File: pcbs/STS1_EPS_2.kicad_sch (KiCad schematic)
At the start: 8 parts, among them J1 Inter-EPS, J2 DS1, J3 DS2, J4 DS3, J5 DS4, J6 RBF, J7 Antenna Deployment, J8 UCI

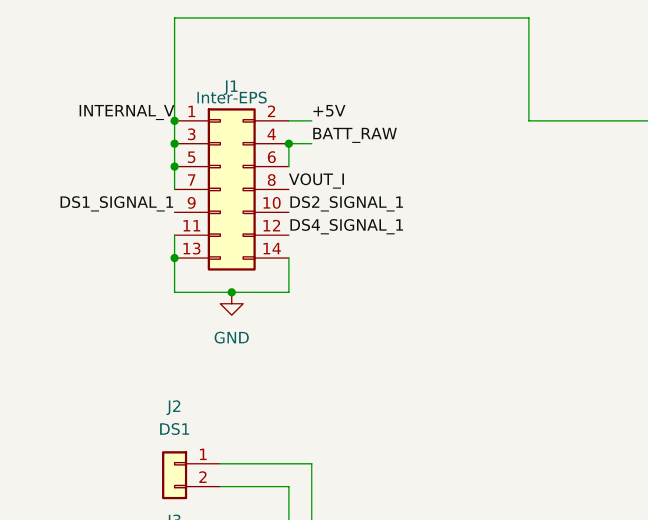
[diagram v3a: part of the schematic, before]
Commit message: Made STS1_EPS_2 inter EPS connector consistent to STS1_EPS_1.
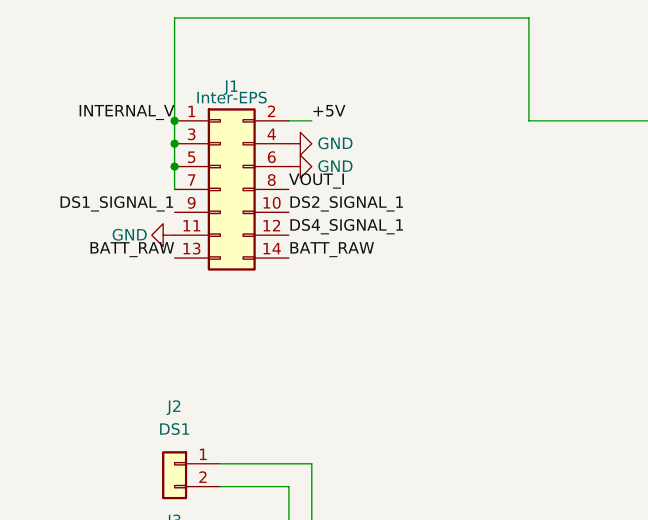
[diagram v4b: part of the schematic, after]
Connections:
- net BATT_RAW: now also J1.13 (Pin_13), J1.14 (Pin_14); no longer J1.4 (Pin_4), J1.6 (Pin_6)
- net GND: now also J1.4 (Pin_4), J1.6 (Pin_6); no longer J1.13 (Pin_13), J1.14 (Pin_14)
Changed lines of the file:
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@@
 (kicad_sch (version 20211123) (generator eeschema)
   (paper "A4")
-  (junction (at 40.64 45.72) (diameter 0) (color 0 0 0 0)
-  )
-  (junction (at 27.94 58.42) (diameter 0) (color 0 0 0 0)
-  )
   (junction (at 27.94 48.26) (diameter 0) (color 0 0 0 0)
   )
@@
   )
   (junction (at 27.94 43.18) (diameter 0) (color 0 0 0 0)
-  )
-  (junction (at 34.29 62.23) (diameter 0) (color 0 0 0 0)
   )
   (no_connect (at 43.18 185.42))
@@
     (stroke (width 0) (type default) (color 0 0 0 0))
   )
-  (wire (pts (xy 27.94 62.23) (xy 34.29 62.23))
-    (stroke (width 0) (type default) (color 0 0 0 0))
-  )
   (wire (pts (xy 40.64 43.18) (xy 43.18 43.18))
     (stroke (width 0) (type default) (color 0 0 0 0))
   )
-  (wire (pts (xy 27.94 58.42) (xy 27.94 62.23))
-    (stroke (width 0) (type default) (color 0 0 0 0))
-  )
   (wire (pts (xy 33.02 109.22) (xy 49.53 109.22))
     (stroke (width 0) (type default) (color 0 0 0 0))
@@
     (stroke (width 0) (type default) (color 0 0 0 0))
   )
-  (wire (pts (xy 43.18 45.72) (xy 40.64 45.72))
-    (stroke (width 0) (type default) (color 0 0 0 0))
-  )
   (wire (pts (xy 27.94 43.18) (xy 27.94 31.75))
     (stroke (width 0) (type default) (color 0 0 0 0))
@@
     (stroke (width 0) (type default) (color 0 0 0 0))
   )
-  (wire (pts (xy 27.94 55.88) (xy 27.94 58.42))
-    (stroke (width 0) (type default) (color 0 0 0 0))
-  )
-  (wire (pts (xy 40.64 58.42) (xy 40.64 62.23))
-    (stroke (width 0) (type default) (color 0 0 0 0))
-  )
   (wire (pts (xy 33.02 121.92) (xy 38.1 121.92))
     (stroke (width 0) (type default) (color 0 0 0 0))
@@
     (stroke (width 0) (type default) (color 0 0 0 0))
   )
-  (wire (pts (xy 40.64 62.23) (xy 34.29 62.23))
-    (stroke (width 0) (type default) (color 0 0 0 0))
-  )
   (wire (pts (xy 33.02 96.52) (xy 35.56 96.52))
     (stroke (width 0) (type default) (color 0 0 0 0))
   )
-  (wire (pts (xy 40.64 45.72) (xy 40.64 48.26))
-    (stroke (width 0) (type default) (color 0 0 0 0))
-  )
   (wire (pts (xy 40.64 120.65) (xy 49.53 120.65))
     (stroke (width 0) (type default) (color 0 0 0 0))
@@
     (effects (font (size 1.27 1.27)) (justify left bottom))
   )
+  (label "BATT_RAW" (at 40.64 58.42 0)
+    (effects (font (size 1.27 1.27)) (justify left bottom))
+  )
   (label "DS3_SIGNAL_2" (at 78.74 111.76 0)
     (effects (font (size 1.27 1.27)) (justify left bottom))
   )
-  (label "BATT_RAW" (at 43.18 45.72 0)
-    (effects (font (size 1.27 1.27)) (justify left bottom))
-  )
   (label "UCI_COBC_UART_[1..2]" (at 240.03 53.34 180)
     (effects (font (size 1.27 1.27)) (justify right bottom))
@@
   )
   (label "DS3_SIGNAL_1" (at 168.91 49.53 180)
+    (effects (font (size 1.27 1.27)) (justify right bottom))
+  )
+  (label "BATT_RAW" (at 27.94 58.42 180)
     (effects (font (size 1.27 1.27)) (justify right bottom))
   )
@@
     (pin "4")
   )
-  (symbol (lib_id "power:GND") (at 34.29 62.23 0) (unit 1)
+  (symbol (lib_id "power:GND") (at 40.64 48.26 90) (unit 1)
     (in_bom yes) (on_board yes) (fields_autoplaced)
-    (property "Reference" "#PWR0101" (id 0) (at 34.29 68.58 0)
-      (effects (font (size 1.27 1.27)) hide)
-    )
-    (property "Value" "GND" (id 1) (at 34.29 67.31 0))
-    (property "Footprint" "" (id 2) (at 34.29 62.23 0)
-      (effects (font (size 1.27 1.27)) hide)
-    )
-    (property "Datasheet" "" (id 3) (at 34.29 62.23 0)
+    (property "Reference" "#PWR?" (id 0) (at 46.99 48.26 0)
+      (effects (font (size 1.27 1.27)) hide)
+    )
+    (property "Value" "GND" (id 1) (at 43.815 48.2599 90)
+      (effects (font (size 1.27 1.27)) (justify right))
+    )
+    (property "Footprint" "" (id 2) (at 40.64 48.26 0)
+      (effects (font (size 1.27 1.27)) hide)
+    )
+    (property "Datasheet" "" (id 3) (at 40.64 48.26 0)
+      (effects (font (size 1.27 1.27)) hide)
+    )
+    (pin "1")
+  )
+  (symbol (lib_id "power:GND") (at 40.64 45.72 90) (unit 1)
+    (in_bom yes) (on_board yes) (fields_autoplaced)
+    (property "Reference" "#PWR?" (id 0) (at 46.99 45.72 0)
+      (effects (font (size 1.27 1.27)) hide)
+    )
+    (property "Value" "GND" (id 1) (at 43.815 45.7199 90)
+      (effects (font (size 1.27 1.27)) (justify right))
+    )
+    (property "Footprint" "" (id 2) (at 40.64 45.72 0)
+      (effects (font (size 1.27 1.27)) hide)
+    )
+    (property "Datasheet" "" (id 3) (at 40.64 45.72 0)
       (effects (font (size 1.27 1.27)) hide)
     )
@@
     (pin "2")
   )
+  (symbol (lib_id "power:GND") (at 27.94 55.88 270) (unit 1)
+    (in_bom yes) (on_board yes)
+    (property "Reference" "#PWR?" (id 0) (at 21.59 55.88 0)
+      (effects (font (size 1.27 1.27)) hide)
+    )
+    (property "Value" "GND" (id 1) (at 20.955 55.88 90)
+      (effects (font (size 1.27 1.27)) (justify left))
+    )
+    (property "Footprint" "" (id 2) (at 27.94 55.88 0)
+      (effects (font (size 1.27 1.27)) hide)
+    )
+    (property "Datasheet" "" (id 3) (at 27.94 55.88 0)
+      (effects (font (size 1.27 1.27)) hide)
+    )
+    (pin "1")
+  )
   (symbol (lib_id "Connector_Generic:Conn_01x02") (at 27.94 93.98 0) (mirror y) (unit 1)
     (in_bom yes) (on_board yes) (fields_autoplaced)
@@
       (reference "#PWR089") (unit 1) (value "GND") (footprint "")
     )
-    (path "/97f7ae26-9f01-48e3-86f9-e28337f57314"
-      (reference "#PWR0101") (unit 1) (value "GND") (footprint "")
-    )
     (path "/d08cc104-26df-403e-aeed-bb3c2e21e328/08a55943-56b2-44aa-a3f3-c51c6cdeff77"
       (reference "#PWR0102") (unit 1) (value "GND") (footprint "")
@@
       (reference "#PWR0104") (unit 1) (value "GND") (footprint "")
     )
+    (path "/81fc32f2-1bea-4d85-b273-19aea6694f98"
+      (reference "#PWR?") (unit 1) (value "GND") (footprint "")
+    )
+    (path "/aa4cb8ae-1732-4508-8f86-241f5fda7b1d"
+      (reference "#PWR?") (unit 1) (value "GND") (footprint "")
+    )
+    (path "/d6440847-fffc-4688-9eb9-ddd3a0cae49d"
+      (reference "#PWR?") (unit 1) (value "GND") (footprint "")
+    )
     (path "/d08cc104-26df-403e-aeed-bb3c2e21e328/f818a80f-c894-4935-b466-2fb75a773837"

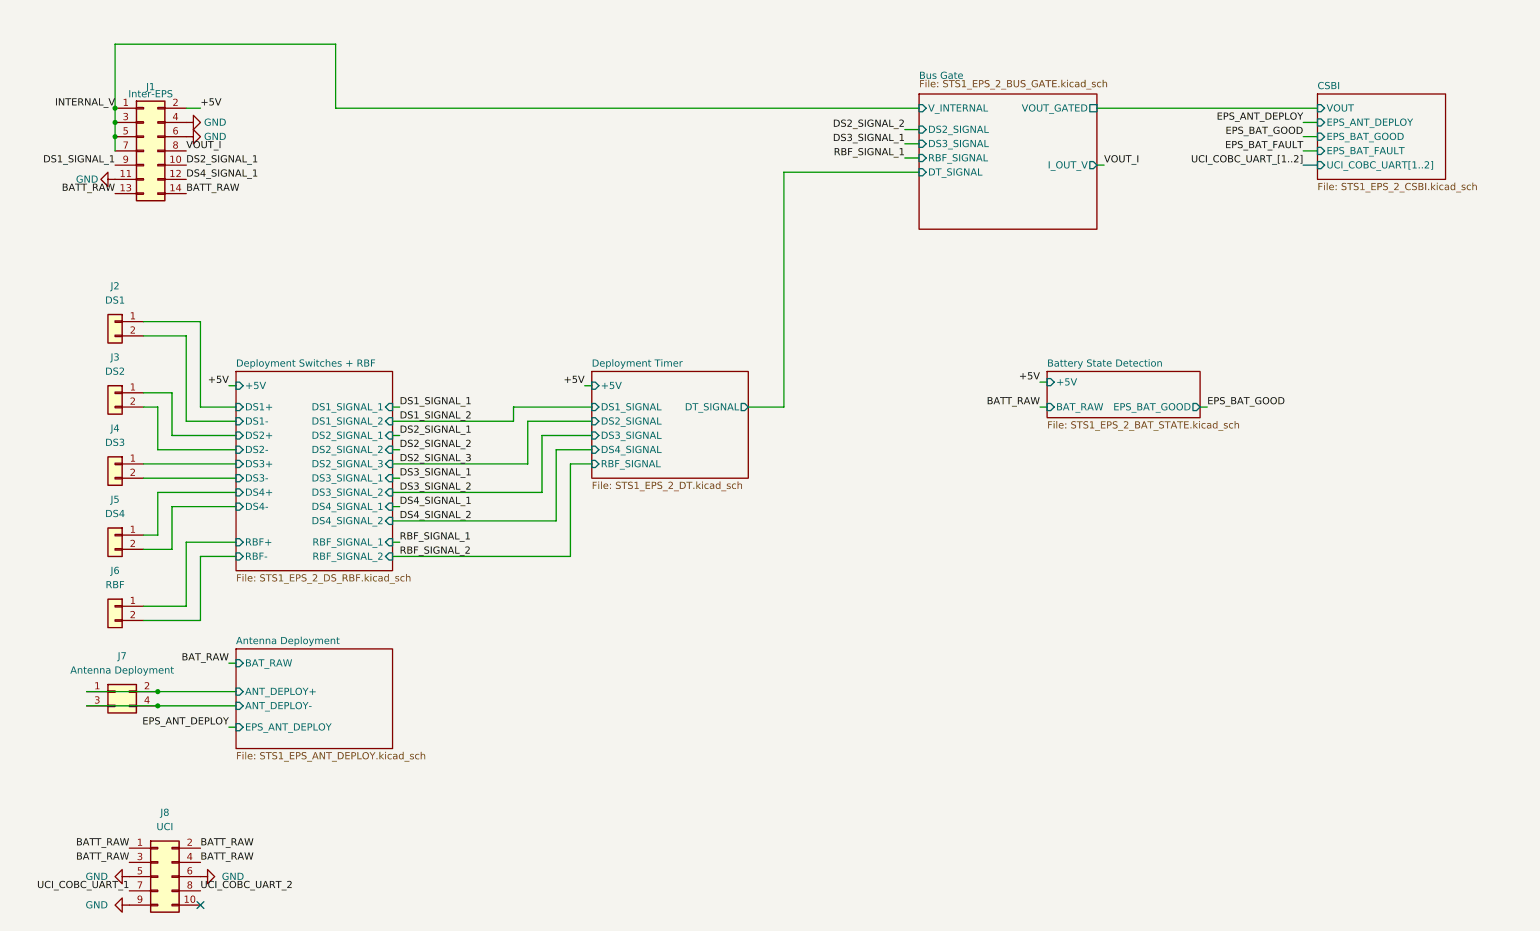
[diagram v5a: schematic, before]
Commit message: Reworked STS1_EPS_2. - Added Capacitor bank - Thickened some load bearing copper traces.
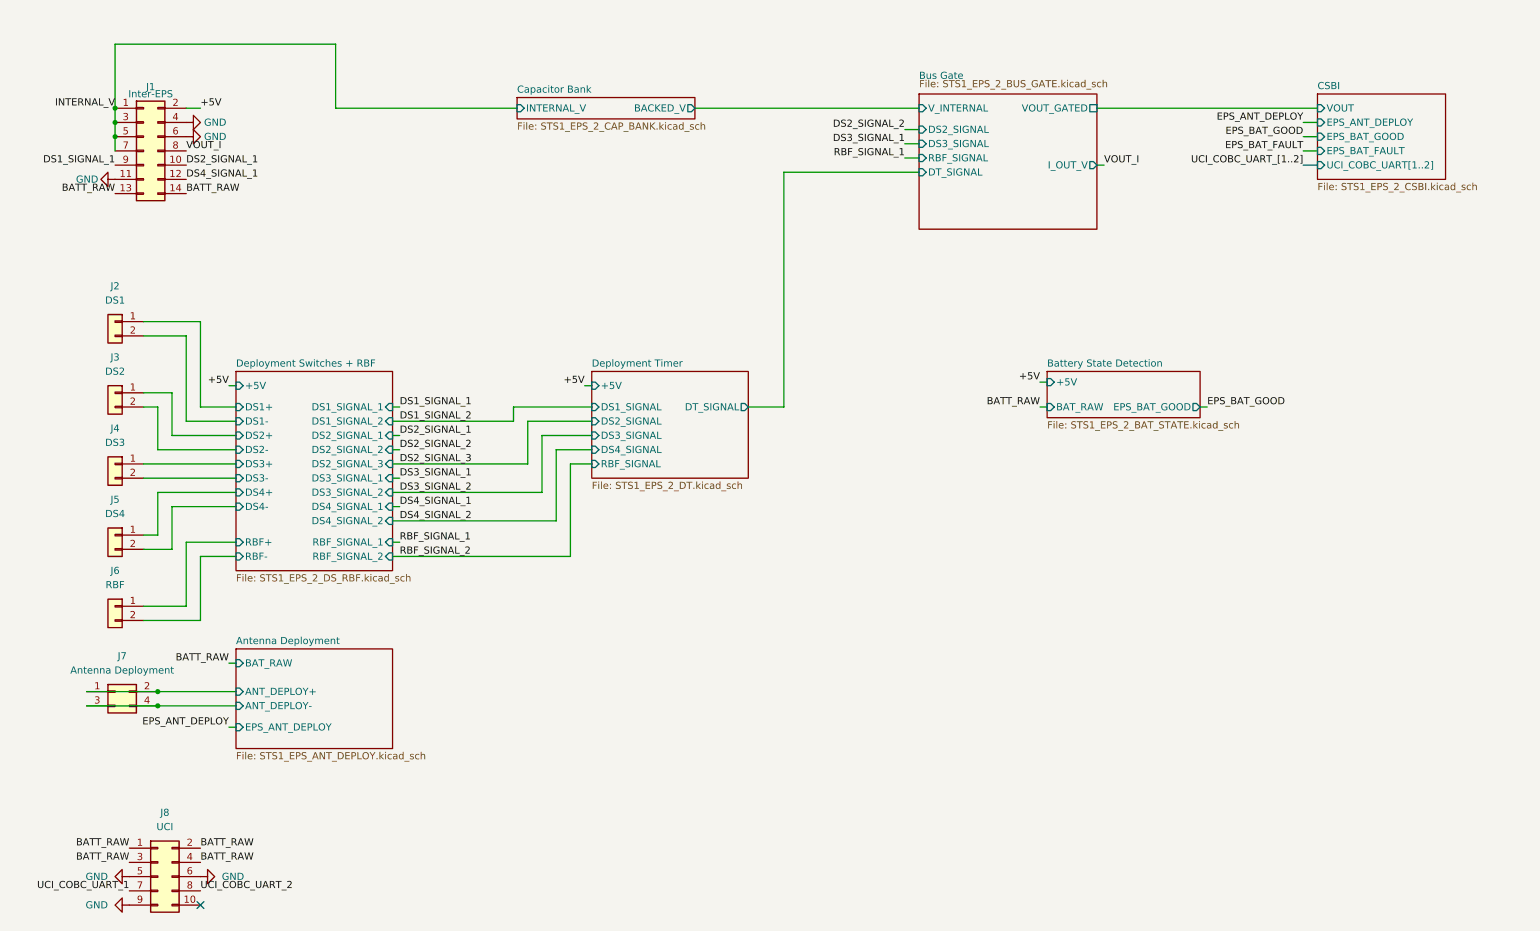
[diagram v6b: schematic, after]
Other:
- added sheet Capacitor Bank (STS1_EPS_2_CAP_BANK.kicad_sch)
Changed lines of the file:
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@@
+    (stroke (width 0) (type default) (color 0 0 0 0))
+  )
+  (wire (pts (xy 131.445 43.18) (xy 171.45 43.18))
     (stroke (width 0) (type default) (color 0 0 0 0))
   )
@@
     (stroke (width 0) (type default) (color 0 0 0 0))
   )
+  (wire (pts (xy 99.695 43.18) (xy 67.31 43.18))
+    (stroke (width 0) (type default) (color 0 0 0 0))
+  )
   (wire (pts (xy 43.18 134.62) (xy 43.18 123.19))
     (stroke (width 0) (type default) (color 0 0 0 0))
@@
     (stroke (width 0) (type default) (color 0 0 0 0))
   )
-  (wire (pts (xy 67.31 43.18) (xy 171.45 43.18))
-    (stroke (width 0) (type default) (color 0 0 0 0))
-  )
   (wire (pts (xy 38.1 101.6) (xy 49.53 101.6))
     (stroke (width 0) (type default) (color 0 0 0 0))
@@
     (effects (font (size 1.27 1.27)) (justify right bottom))
   )
-  (label "BAT_RAW" (at 48.26 142.24 180)
+  (label "BATT_RAW" (at 48.26 142.24 180)
     (effects (font (size 1.27 1.27)) (justify right bottom))
   )
@@
     )
   )
+  (sheet (at 99.695 41.275) (size 31.75 3.81) (fields_autoplaced)
+    (stroke (width 0.1524) (type solid) (color 0 0 0 0))
+    (fill (color 255 255 0 1.0000))
+    (property "Sheet name" "Capacitor Bank" (id 0) (at 99.695 40.5634 0)
+      (effects (font (size 1.27 1.27)) (justify left bottom))
+    )
+    (property "Sheet file" "STS1_EPS_2_CAP_BANK.kicad_sch" (id 1) (at 99.695 45.6696 0)
+      (effects (font (size 1.27 1.27)) (justify left top))
+    )
+    (pin "INTERNAL_V" input (at 99.695 43.18 180)
+      (effects (font (size 1.27 1.27)) (justify left))
+    )
+    (pin "BACKED_V" output (at 131.445 43.18 0)
+      (effects (font (size 1.27 1.27)) (justify right))
+    )
+  )
   (sheet (at 194.31 90.17) (size 27.305 8.255) (fields_autoplaced)
     (stroke (width 0.1524) (type solid) (color 0 0 0 0))
@@
     (path "/f6013889-7b77-4458-9ae4-3903f8947363" (page "6"))
     (path "/975ef3b6-1008-4d19-83f6-e886243dad51" (page "7"))
+    (path "/f1424bad-2b95-4d34-bc23-e338e9fb6fbb" (page "8"))
   )
   (symbol_instances
@@
       (reference "#PWR054") (unit 1) (value "GND") (footprint "")
     )
+    (path "/f1424bad-2b95-4d34-bc23-e338e9fb6fbb/13001122-9f7b-43c3-9cd6-371a20f82a80"
+      (reference "#PWR055") (unit 1) (value "GND") (footprint "")
+    )
+    (path "/f1424bad-2b95-4d34-bc23-e338e9fb6fbb/c21bfdab-2dbd-4005-9d4d-c0f43b63b038"
+      (reference "#PWR056") (unit 1) (value "GND") (footprint "")
+    )
+    (path "/f1424bad-2b95-4d34-bc23-e338e9fb6fbb/9ef7a3ec-23f3-4ac7-9b08-342500594731"
+      (reference "#PWR057") (unit 1) (value "GND") (footprint "")
+    )
+    (path "/f1424bad-2b95-4d34-bc23-e338e9fb6fbb/34315873-e1af-41b7-b231-ae4abdb02aa7"
+      (reference "#PWR058") (unit 1) (value "GND") (footprint "")
+    )
+    (path "/f1424bad-2b95-4d34-bc23-e338e9fb6fbb/b6da7ff9-8d77-4115-b71a-43f45a813e0c"
+      (reference "#PWR059") (unit 1) (value "GND") (footprint "")
+    )
+    (path "/f1424bad-2b95-4d34-bc23-e338e9fb6fbb/12b8c6ff-7483-4f98-982b-64a09013cc09"
+      (reference "#PWR060") (unit 1) (value "GND") (footprint "")
+    )
+    (path "/f1424bad-2b95-4d34-bc23-e338e9fb6fbb/df9adae2-19f6-4079-9357-1ac16edbe82f"
+      (reference "#PWR061") (unit 1) (value "GND") (footprint "")
+    )
+    (path "/f1424bad-2b95-4d34-bc23-e338e9fb6fbb/f59ab91b-3873-4e0d-8e76-309adc34e8ad"
+      (reference "#PWR062") (unit 1) (value "GND") (footprint "")
+    )
+    (path "/f1424bad-2b95-4d34-bc23-e338e9fb6fbb/383ee479-7cb6-4308-bda4-2db98e15e246"
+      (reference "#PWR063") (unit 1) (value "GND") (footprint "")
+    )
+    (path "/f1424bad-2b95-4d34-bc23-e338e9fb6fbb/6587fd9e-c92c-40a6-9b44-08d30c1591f7"
+      (reference "#PWR064") (unit 1) (value "GND") (footprint "")
+    )
+    (path "/f1424bad-2b95-4d34-bc23-e338e9fb6fbb/fde8fff5-656e-431d-93fc-1003e8df912c"
+      (reference "#PWR065") (unit 1) (value "GND") (footprint "")
+    )
+    (path "/f1424bad-2b95-4d34-bc23-e338e9fb6fbb/e14abb33-d113-43eb-8f7e-1d73c17f0fc5"
+      (reference "#PWR066") (unit 1) (value "GND") (footprint "")
+    )
+    (path "/f1424bad-2b95-4d34-bc23-e338e9fb6fbb/0694a10a-d8da-48a3-b260-f97da1e700fd"
+      (reference "#PWR067") (unit 1) (value "GND") (footprint "")
+    )
+    (path "/f1424bad-2b95-4d34-bc23-e338e9fb6fbb/4654fb7e-8526-4edf-9b7f-34d2719c3a74"
+      (reference "#PWR068") (unit 1) (value "GND") (footprint "")
+    )
+    (path "/f1424bad-2b95-4d34-bc23-e338e9fb6fbb/5b9d4dea-f51b-4891-acb6-d037458505db"
+      (reference "#PWR069") (unit 1) (value "GND") (footprint "")
+    )
+    (path "/f1424bad-2b95-4d34-bc23-e338e9fb6fbb/8e498e40-ec1c-494a-b618-f427264a6574"
+      (reference "#PWR070") (unit 1) (value "GND") (footprint "")
+    )
     (path "/4a4cf4f3-b3ca-46d9-b2ff-f21a8c4df335/cfc68ce3-6fc8-4636-977e-f459f51d4fdc"
       (reference "#PWR081") (unit 1) (value "GND") (footprint "")
@@
       (reference "C5") (unit 1) (value "100n") (footprint "Capacitor_SMD:C_0805_2012Metric")
     )
+    (path "/f1424bad-2b95-4d34-bc23-e338e9fb6fbb/723f186f-e509-4f79-b697-dbc3026f5475"
+      (reference "C6") (unit 1) (value "C_Polarized") (footprint "Capacitor_Tantalum_SMD:CP_EIA-7343-43_Kemet-X")
+    )
+    (path "/f1424bad-2b95-4d34-bc23-e338e9fb6fbb/b1760b00-bfac-4a83-8ee9-c2f1bfd2d1f9"
+      (reference "C7") (unit 1) (value "C") (footprint "Capacitor_SMD:C_0805_2012Metric")
+    )
+    (path "/f1424bad-2b95-4d34-bc23-e338e9fb6fbb/f6ed493f-e121-427f-a2ef-45fec099a83b"
+      (reference "C8") (unit 1) (value "C") (footprint "Capacitor_SMD:C_0805_2012Metric")
+    )
+    (path "/f1424bad-2b95-4d34-bc23-e338e9fb6fbb/e0e4504f-53f9-4186-9cf0-5f5692dade37"
+      (reference "C9") (unit 1) (value "C") (footprint "Capacitor_SMD:C_0805_2012Metric")
+    )
+    (path "/f1424bad-2b95-4d34-bc23-e338e9fb6fbb/6a609d22-4e4e-4b0a-9f7a-81951b5fa963"
+      (reference "C10") (unit 1) (value "C_Polarized") (footprint "Capacitor_Tantalum_SMD:CP_EIA-7343-43_Kemet-X")
+    )
+    (path "/f1424bad-2b95-4d34-bc23-e338e9fb6fbb/ec6df8a7-950d-4da9-9729-0fcf78f40e28"
+      (reference "C11") (unit 1) (value "C") (footprint "Capacitor_SMD:C_0805_2012Metric")
+    )
+    (path "/f1424bad-2b95-4d34-bc23-e338e9fb6fbb/212e8519-c4b5-4595-8229-b1c4277c4f37"
+      (reference "C12") (unit 1) (value "C") (footprint "Capacitor_SMD:C_0805_2012Metric")
+    )
+    (path "/f1424bad-2b95-4d34-bc23-e338e9fb6fbb/b2ed7dd8-3df9-4cc2-a304-b76acaec94bc"
+      (reference "C13") (unit 1) (value "C_Polarized") (footprint "Capacitor_Tantalum_SMD:CP_EIA-7343-43_Kemet-X")
+    )
+    (path "/f1424bad-2b95-4d34-bc23-e338e9fb6fbb/5c66b8e1-b79a-4cff-b6c3-acfed3cf5ae1"
+      (reference "C14") (unit 1) (value "C") (footprint "Capacitor_SMD:C_0805_2012Metric")
+    )
+    (path "/f1424bad-2b95-4d34-bc23-e338e9fb6fbb/1e60eeae-2139-4b4d-9a5c-78a8982d7e29"
+      (reference "C15") (unit 1) (value "C") (footprint "Capacitor_SMD:C_0805_2012Metric")
+    )
+    (path "/f1424bad-2b95-4d34-bc23-e338e9fb6fbb/9704fb47-fef8-4b6d-ada7-99cc254ed926"
+      (reference "C16") (unit 1) (value "C_Polarized") (footprint "Capacitor_Tantalum_SMD:CP_EIA-7343-43_Kemet-X")
+    )
+    (path "/f1424bad-2b95-4d34-bc23-e338e9fb6fbb/b4121b47-f7c9-43d3-8a0e-2fd48447831d"
+      (reference "C17") (unit 1) (value "C") (footprint "Capacitor_SMD:C_0805_2012Metric")
+    )
+    (path "/f1424bad-2b95-4d34-bc23-e338e9fb6fbb/54ec4744-d942-4ba6-a87b-b8c60bfb75f8"
+      (reference "C18") (unit 1) (value "C") (footprint "Capacitor_SMD:C_0805_2012Metric")
+    )
+    (path "/f1424bad-2b95-4d34-bc23-e338e9fb6fbb/cda492c7-7d76-4ced-952b-f2800c1db58b"
+      (reference "C19") (unit 1) (value "C_Polarized") (footprint "Capacitor_Tantalum_SMD:CP_EIA-7343-43_Kemet-X")
+    )
+    (path "/f1424bad-2b95-4d34-bc23-e338e9fb6fbb/d4e47442-5155-44e0-88cf-fcdd2d5213e9"
+      (reference "C20") (unit 1) (value "C") (footprint "Capacitor_SMD:C_0805_2012Metric")
+    )
+    (path "/f1424bad-2b95-4d34-bc23-e338e9fb6fbb/8299084d-fb7b-4316-b7e8-0f44cd67c851"
+      (reference "C21") (unit 1) (value "C") (footprint "Capacitor_SMD:C_0805_2012Metric")
+    )
     (path "/4a4cf4f3-b3ca-46d9-b2ff-f21a8c4df335/59e947b1-e254-4558-91bc-1318a7ec413c"
